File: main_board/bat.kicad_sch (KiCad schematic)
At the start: 50 parts, among them IC1 MP2722GRH-0000-Z, IC2 MP3429GL-Z, IC3 NX3DV42GU, J4 USB_B_Micro, J5 USB_C_Receptacle_USB2.0, U3 ATmega32U4-M, U5 AP2204RB-3.3, U7 INA220AIDGST, Y1 Crystal

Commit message: Rev 1 draft
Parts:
- removed IC3: NX3DV42GU, 000_custom:NX3DV42GU, symbol 000_Custom:NX3DV42GU
- added C65, C66, C67: 1u, Capacitor_SMD:C_0805_2012Metric_Pad1.18x1.45mm_HandSolder, symbol Device:C
- added MOSFET1: STL9P3LLH6, POWERFLAT_3P3X3P3_STM, symbol 000_Custom:STL9P3LLH6
- added R23: 1K, Resistor_SMD:R_0805_2012Metric_Pad1.20x1.40mm_HandSolder, symbol Device:R
- added U8: STUSB4500QTR, 000_custom:STUSB4500, symbol 000_Custom:STUSB4500QTR
- R5: value 0R -> 100K; Field6 (none) -> MCR01MZPF1002; Field7 (none) -> Rohm; Part Description Resistor 2.2K M1005 1% 63mW -> Resistor 10K M1005 1% 63mW
- R9: value 2.2K 1% -> 10K; Field6 (none) -> MCR01MZPF1002; Field7 (none) -> Rohm; Part Description Resistor 2.2K M1005 1% 63mW -> Resistor 10K M1005 1% 63mW; now fitted; now in the parts list
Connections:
- net GND: now also C65.2, C66.2, C67.2, U8.10 (GND), U8.12 (ADDR0), U8.13 (ADDR1), U8.22 (VSYS), U8.25 (EP), U8.6 (RESET), U8.9 (DISCH); no longer R9.2
- net IIC_SCL: now also U8.7 (SCL)
- net IIC_SDA: now also U8.8 (SDA)
- net CC1: no longer names the net of J5.A5 (CC1)
- net CC1: now also U8.1 (CC1DB), U8.2 (CC1); no longer IC1.1 (CC1)
- net CC2: no longer names the net of J5.B5 (CC2)
- net CC2: now also U8.4 (CC2), U8.5 (CC2DB); no longer IC1.22 (CC2_1)
- net OTG_SW: no longer names the net of U3.29 (PB5)
- net PMIC INTERRUPT: no longer names the net of IC1.8 (~{INT})
- net PMIC INTERRUPT: no longer U3.28 (PB4)
- removed net USB2_N: J5.A7 (D-), J5.B7 (D-), R5.1, R5.2
- net USB2_P: no longer names the net of J5.A6 (D+)
- net USB2_P: no longer J5.B6 (D+)
- net USBC_MX2_USB2_N: no longer names the net of IC1.20 (D-)
- net USBC_MX2_USB2_P: no longer names the net of IC1.21 (D+)
- net USB_SW_VCC: no longer names the net of U3.30 (PB6)
- net VIN: no longer names the net of J5.A4 (VBUS), J5.A9 (VBUS), J5.B4 (VBUS), J5.B9 (VBUS)
- net VIN: now also R5.1, C67.1, MOSFET1.1 (S), MOSFET1.2 (S), MOSFET1.3 (S), R23.1, U8.24 (VDD); no longer C19.1, IC1.2 (IN), R9.1
- new net: MOSFET1.4 (G), R5.2, R9.1
- new net: R9.2, U8.16 (VBUS_EN_SNK)
- new net: R23.2, U8.18 (VBUS_VS_DISCH)
- new net: C65.1, U8.21 (VREG_1V2)
- new net: C66.1, U8.23 (VREG_2V7)
- new net: C19.1, IC1.2 (IN), MOSFET1.5 (D), MOSFET1.6 (D), MOSFET1.7 (D), MOSFET1.8 (D)
- no-connect marks 7 -> 22
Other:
- note removed: "Discharge Resistor Needed by some Type C PSUs"
- note removed: "P/N swapped for easier routing"
- moved on the sheet: BT1, C17, C19, C20, C21, C22, C23, C24, C25, C26, C27, C28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

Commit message: Final fixes
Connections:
- net GND: now also U3.36 (PF7), U3.37 (PF6), U3.38 (PF5), U3.39 (PF4), U3.40 (PF1)
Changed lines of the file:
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@@
 	)
 	(junction
+		(at 99.06 256.54)
+		(diameter 0)
+		(color 0 0 0 0)
+	)
+	(junction
 		(at 161.29 115.57)
 		(diameter 0)
@@
 	)
 	(junction
+		(at 99.06 254)
+		(diameter 0)
+		(color 0 0 0 0)
+	)
+	(junction
 		(at 369.57 91.44)
 		(diameter 0)
@@
 	)
 	(junction
+		(at 99.06 259.08)
+		(diameter 0)
+		(color 0 0 0 0)
+	)
+	(junction
 		(at 187.96 60.96)
 		(diameter 0)
@@
 	(wire
 		(pts
+			(xy 99.06 256.54) (xy 99.06 259.08)
+		)
+		(stroke
+			(width 0)
+			(type default)
+		)
+	)
+	(wire
+		(pts
 			(xy 238.76 46.99) (xy 238.76 29.21)
 		)
@@
 	(wire
 		(pts
+			(xy 104.14 261.62) (xy 104.14 259.08)
+		)
+		(stroke
+			(width 0)
+			(type default)
+		)
+	)
+	(wire
+		(pts
 			(xy 265.43 139.7) (xy 265.43 111.76)
 		)
@@
 	(wire
 		(pts
+			(xy 99.06 259.08) (xy 99.06 261.62)
+		)
+		(stroke
+			(width 0)
+			(type default)
+		)
+	)
+	(wire
+		(pts
 			(xy 171.45 90.17) (xy 171.45 91.44)
 		)
@@
 	(wire
 		(pts
+			(xy 99.06 251.46) (xy 99.06 254)
+		)
+		(stroke
+			(width 0)
+			(type default)
+		)
+	)
+	(wire
+		(pts
 			(xy 276.86 91.44) (xy 276.86 129.54)
 		)
@@
 	(wire
 		(pts
+			(xy 104.14 259.08) (xy 99.06 259.08)
+		)
+		(stroke
+			(width 0)
+			(type default)
+		)
+	)
+	(wire
+		(pts
 			(xy 82.55 271.78) (xy 83.82 271.78)
 		)
@@
 	(wire
 		(pts
+			(xy 99.06 254) (xy 99.06 256.54)
+		)
+		(stroke
+			(width 0)
+			(type default)
+		)
+	)
+	(wire
+		(pts
 			(xy 96.52 43.18) (xy 87.63 43.18)
 		)
@@
 					(unit 1)
 				)
+			)
+		)
+	)
+	(symbol
+		(lib_id "power:GND")
+		(at 104.14 261.62 0)
+		(unit 1)
+		(exclude_from_sim no)
+		(in_bom yes)
+		(on_board yes)
+		(dnp no)
+		(property "Reference" "#PWR095"
+			(at 104.14 267.97 0)
+			(effects
+				(font
+					(size 1.27 1.27)
+				)
+				(hide yes)
+			)
+		)
+		(property "Value" "GND"
+			(at 104.14 265.43 0)
+			(effects
+				(font
+					(size 1.27 1.27)
+				)
+			)
+		)
+		(property "Footprint" ""
+			(at 104.14 261.62 0)
+			(effects
+				(font
+					(size 1.27 1.27)
+				)
+				(hide yes)
+			)
+		)
+		(property "Datasheet" ""
+			(at 104.14 261.62 0)
+			(effects
+				(font
+					(size 1.27 1.27)
+				)
+				(hide yes)
+			)
+		)
+		(property "Description" "Power symbol creates a global label with name \"GND\" , ground"
+			(at 104.14 261.62 0)
+			(effects
+				(font
+					(size 1.27 1.27)
+				)
+				(hide yes)
+			)
+		)
+		(pin "1"
+		)
+		(instances
+			(project "main_board"
+				(path "/e63e39d7-6ac0-4ffd-8aa3-1841a4541b55/b84f1a66-243e-4389-abcf-18bc380f8da3"
+					(reference "#PWR095")
+					(unit 1)
+				)

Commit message: Also update schematic
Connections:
- net GND: now also U3.20 (PD2), U3.21 (PD3), U3.22 (PD5)
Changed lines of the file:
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@@
+	)
+	(junction
+		(at 99.06 226.06)
+		(diameter 0)
+		(color 0 0 0 0)
 	)
 	(junction
@@
 	)
 	(junction
-		(at 101.6 233.68)
-		(diameter 0)
-		(color 0 0 0 0)
-	)
-	(junction
 		(at 99.06 254)
 		(diameter 0)
@@
 	)
 	(junction
+		(at 99.06 228.6)
+		(diameter 0)
+		(color 0 0 0 0)
+	)
+	(junction
+		(at 99.06 231.14)
+		(diameter 0)
+		(color 0 0 0 0)
+	)
+	(junction
 		(at 355.6 52.07)
 		(diameter 0)
@@
 	(junction
 		(at 260.35 73.66)
+		(diameter 0)
+		(color 0 0 0 0)
+	)
+	(junction
+		(at 99.06 233.68)
 		(diameter 0)
 		(color 0 0 0 0)
@@
 	(wire
 		(pts
+			(xy 99.06 228.6) (xy 99.06 231.14)
+		)
+		(stroke
+			(width 0)
+			(type default)
+		)
+	)
+	(wire
+		(pts
 			(xy 401.32 46.99) (xy 401.32 199.39)
 		)
@@
 	(wire
 		(pts
-			(xy 99.06 236.22) (xy 101.6 236.22)
-		)
-		(stroke
-			(width 0)
-			(type default)
-		)
-	)
-	(wire
-		(pts
 			(xy 261.62 139.7) (xy 265.43 139.7)
 		)
@@
 	(wire
 		(pts
+			(xy 99.06 226.06) (xy 99.06 228.6)
+		)
+		(stroke
+			(width 0)
+			(type default)
+		)
+	)
+	(wire
+		(pts
 			(xy 346.71 73.66) (xy 346.71 81.28)
 		)
@@
 	(wire
 		(pts
-			(xy 101.6 233.68) (xy 101.6 236.22)
-		)
-		(stroke
-			(width 0)
-			(type default)
-		)
-	)
-	(wire
-		(pts
 			(xy 359.41 46.99) (xy 401.32 46.99)
 		)
@@
 	(wire
 		(pts
+			(xy 99.06 231.14) (xy 99.06 233.68)
+		)
+		(stroke
+			(width 0)
+			(type default)
+		)
+	)
+	(wire
+		(pts
 			(xy 193.04 20.32) (xy 190.5 20.32)
 		)
@@
 	(wire
 		(pts
-			(xy 99.06 228.6) (xy 101.6 228.6)
-		)
-		(stroke
-			(width 0)
-			(type default)
-		)
-	)
-	(wire
-		(pts
 			(xy 403.86 201.93) (xy 358.14 201.93)
 		)
@@
 	(wire
 		(pts
+			(xy 99.06 223.52) (xy 99.06 226.06)
+		)
+		(stroke
+			(width 0)
+			(type default)
+		)
+	)
+	(wire
+		(pts
 			(xy 303.53 91.44) (xy 308.61 91.44)
 		)
@@
 	(wire
 		(pts
-			(xy 101.6 228.6) (xy 101.6 233.68)
-		)
-		(stroke
-			(width 0)
-			(type default)
-		)
-	)
-	(wire
-		(pts
 			(xy 99.06 218.44) (xy 168.91 218.44)
 		)
@@
 	(wire
 		(pts
+			(xy 99.06 231.14) (xy 97.79 231.14)
+		)
+		(stroke
+			(width 0)
+			(type default)
+		)
+	)
+	(wire
+		(pts
 			(xy 281.94 29.21) (xy 281.94 36.83)
 		)
@@
 	(wire
 		(pts
-			(xy 101.6 233.68) (xy 106.68 233.68)
-		)
-		(stroke
-			(width 0)
-			(type default)
-		)
-	)
-	(wire
-		(pts
 			(xy 313.69 101.6) (xy 316.23 101.6)
 		)
@@
 	(wire
 		(pts
-			(xy 99.06 233.68) (xy 101.6 233.68)
-		)
-		(stroke
+			(xy 99.06 233.68) (xy 99.06 236.22)
+		)
+		(stroke
+			(width 0)
+			(type default)
+		)
+	)
+	(wire
+		(pts
+			(xy 99.06 233.68) (xy 106.68 233.68)
+		)
+		(stroke

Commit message: Fix fried USB hub
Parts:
- MOSFET1: footprint POWERFLAT_3P3X3P3_STM -> Package_SON:Diodes_PowerDI3333-8
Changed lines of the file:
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@@
 			)
 		)
-		(property "Footprint" "POWERFLAT_3P3X3P3_STM"
+		(property "Footprint" "Package_SON:Diodes_PowerDI3333-8"
 			(at 195.58 20.32 0)
 			(effects

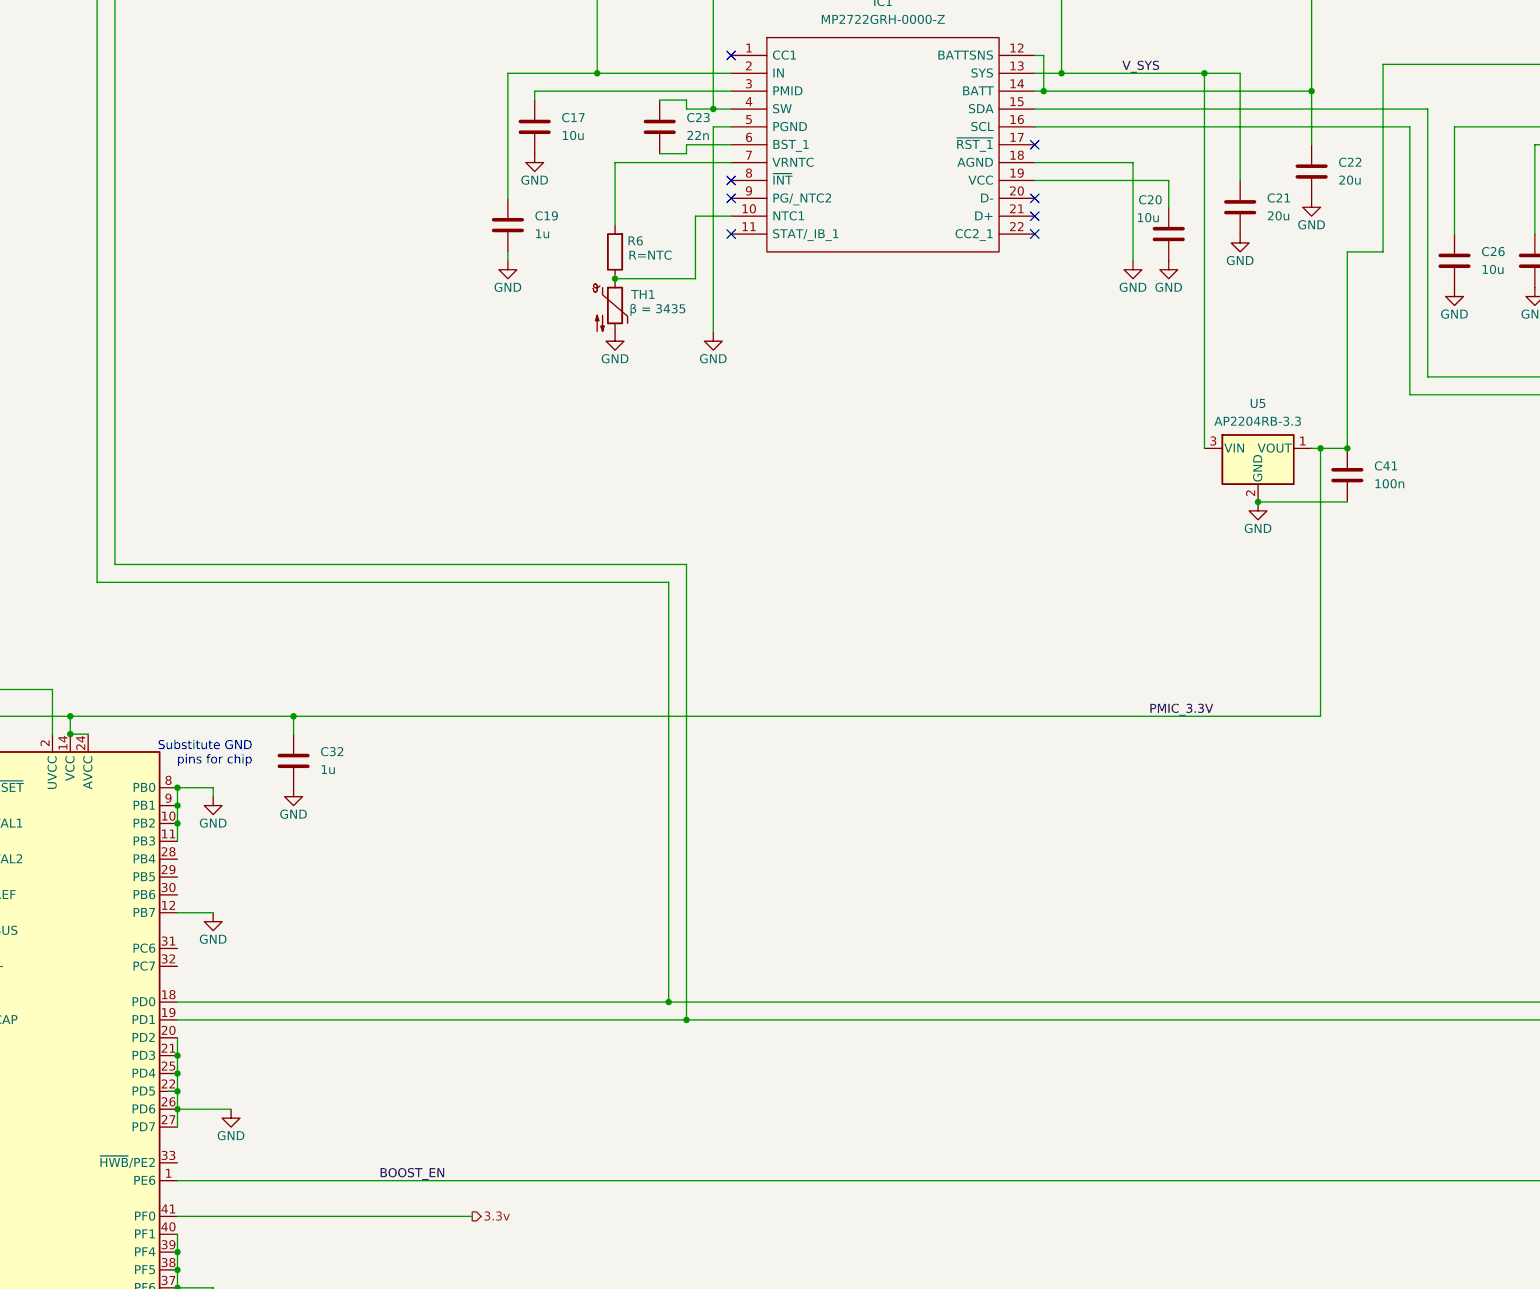
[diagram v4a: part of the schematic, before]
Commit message: Fix 32u4 high power consumption, improve QFN soldering with thick ass solder masks.
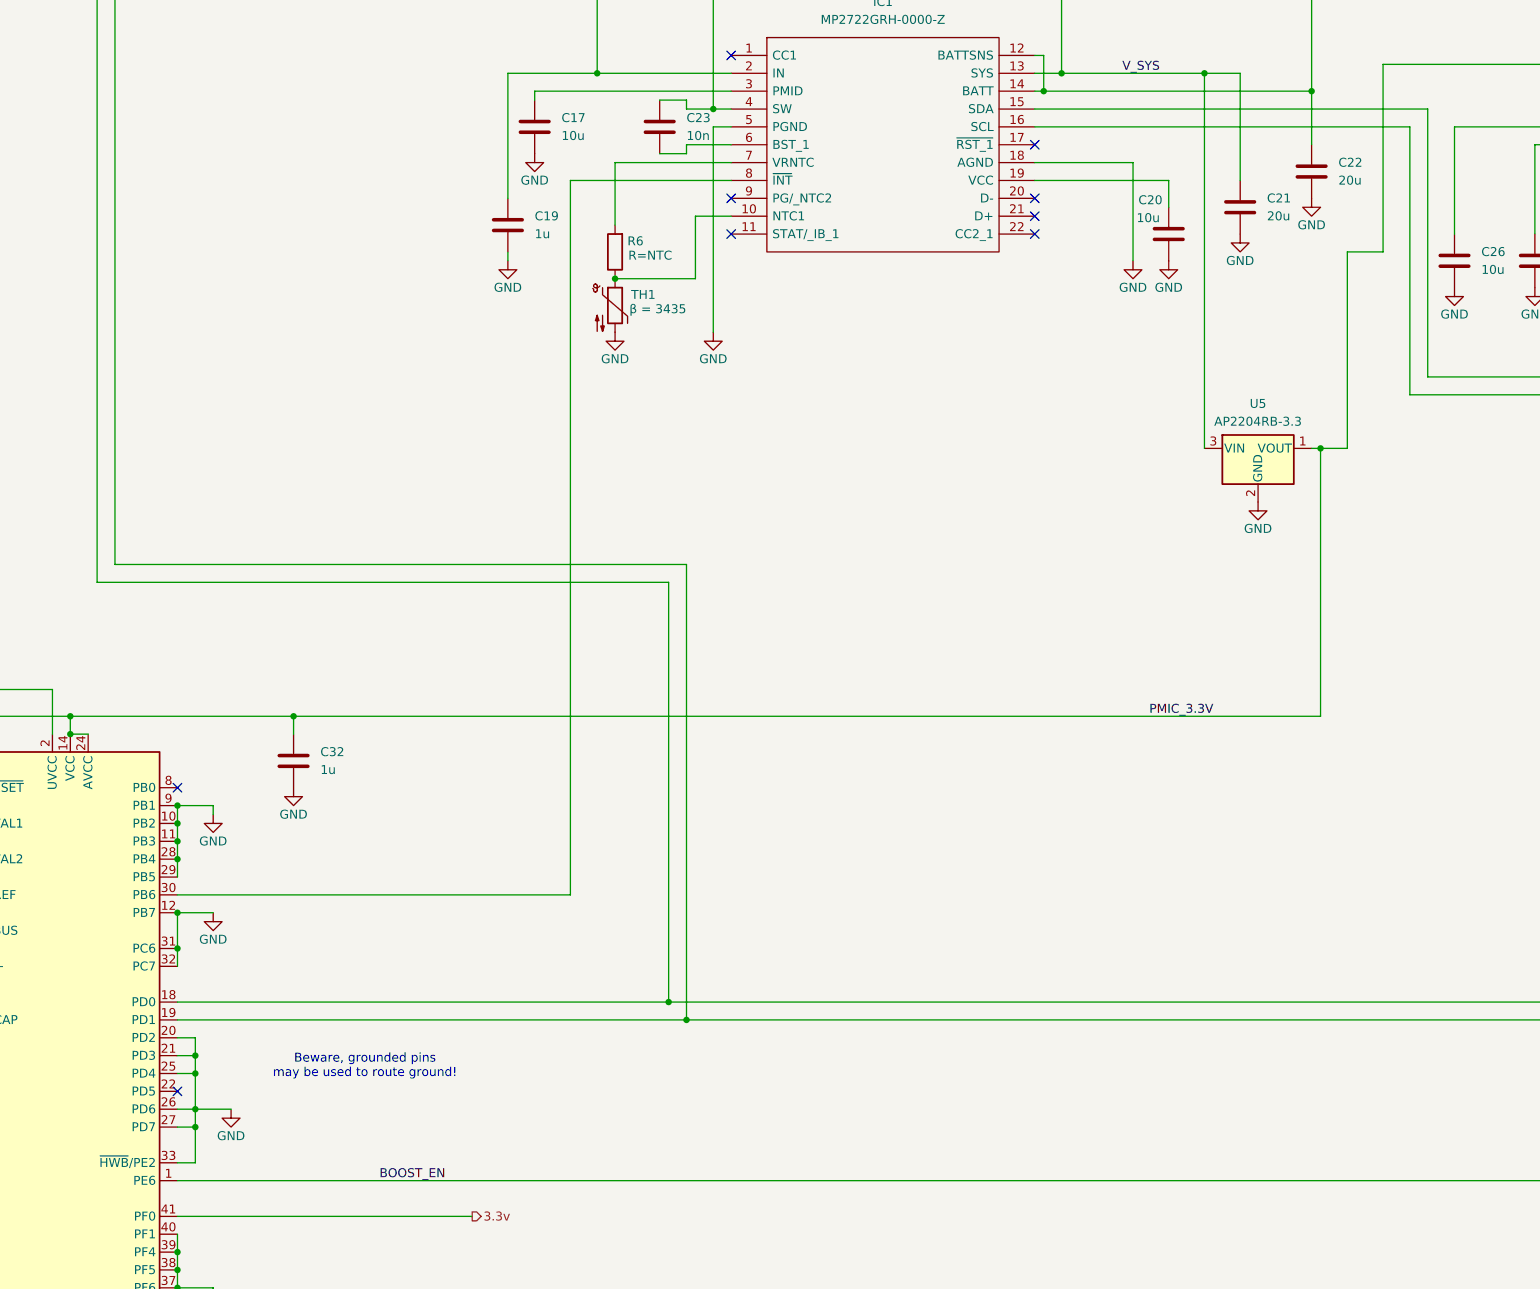
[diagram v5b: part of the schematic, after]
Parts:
- removed C41: 100n, Capacitor_SMD:C_0805_2012Metric_Pad1.18x1.45mm_HandSolder, symbol Device:C
- C23: value 22n -> 10n
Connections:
- net GND: now also U3.28 (PB4), U3.29 (PB5), U3.31 (PC6), U3.32 (PC7), U3.33 (~{HWB}/PE2); no longer U3.22 (PD5), U3.8 (PB0)
- net at IC1.8 (~{INT}): now also U3.30 (PB6)
- no-connect marks 22 -> 23
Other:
- note added: "Beware, grounded pins may be used to route ground!"
- note removed: "Substitute GND pins for chip"

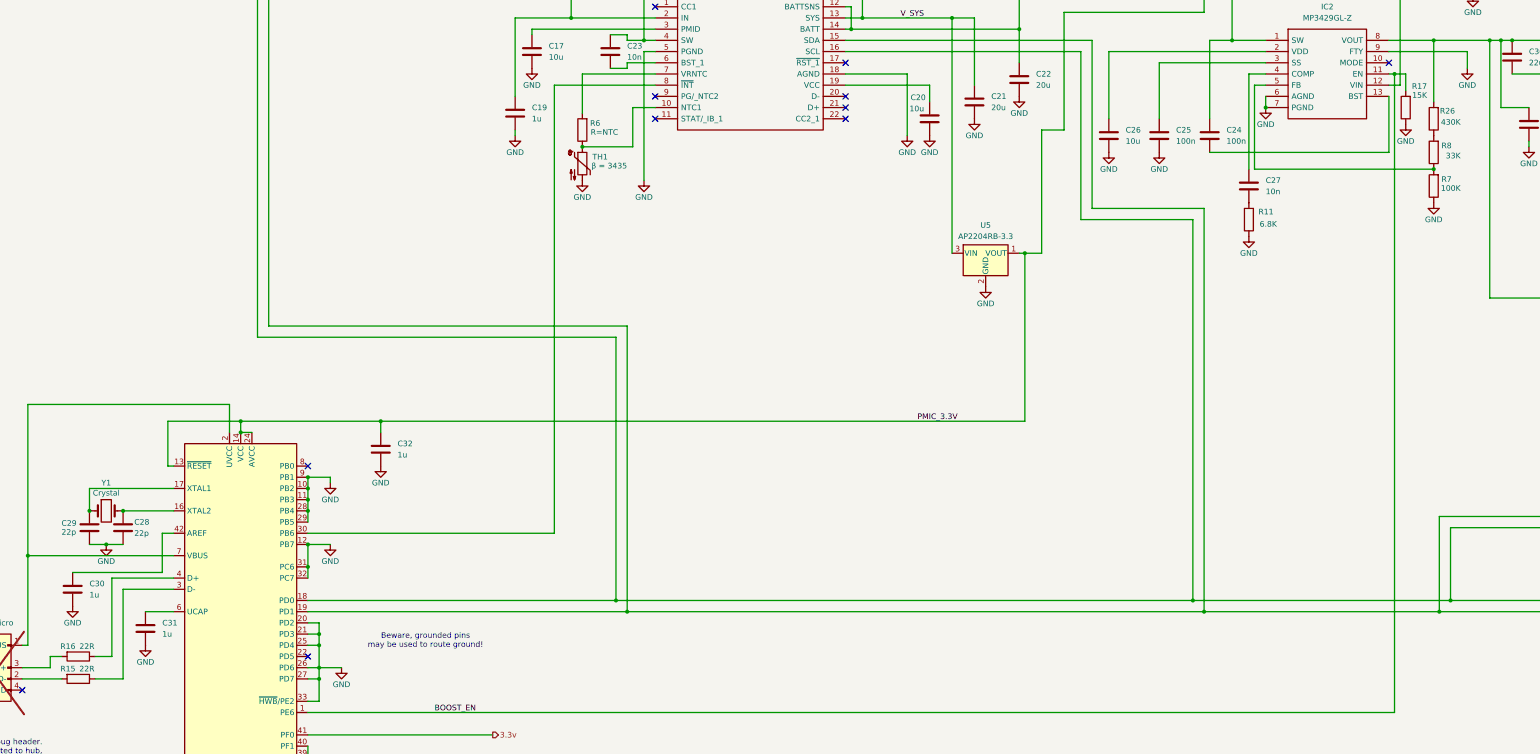
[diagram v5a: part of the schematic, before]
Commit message: Fix bad output voltage
For some reason I got 5V with previous values on prototype. Weird...
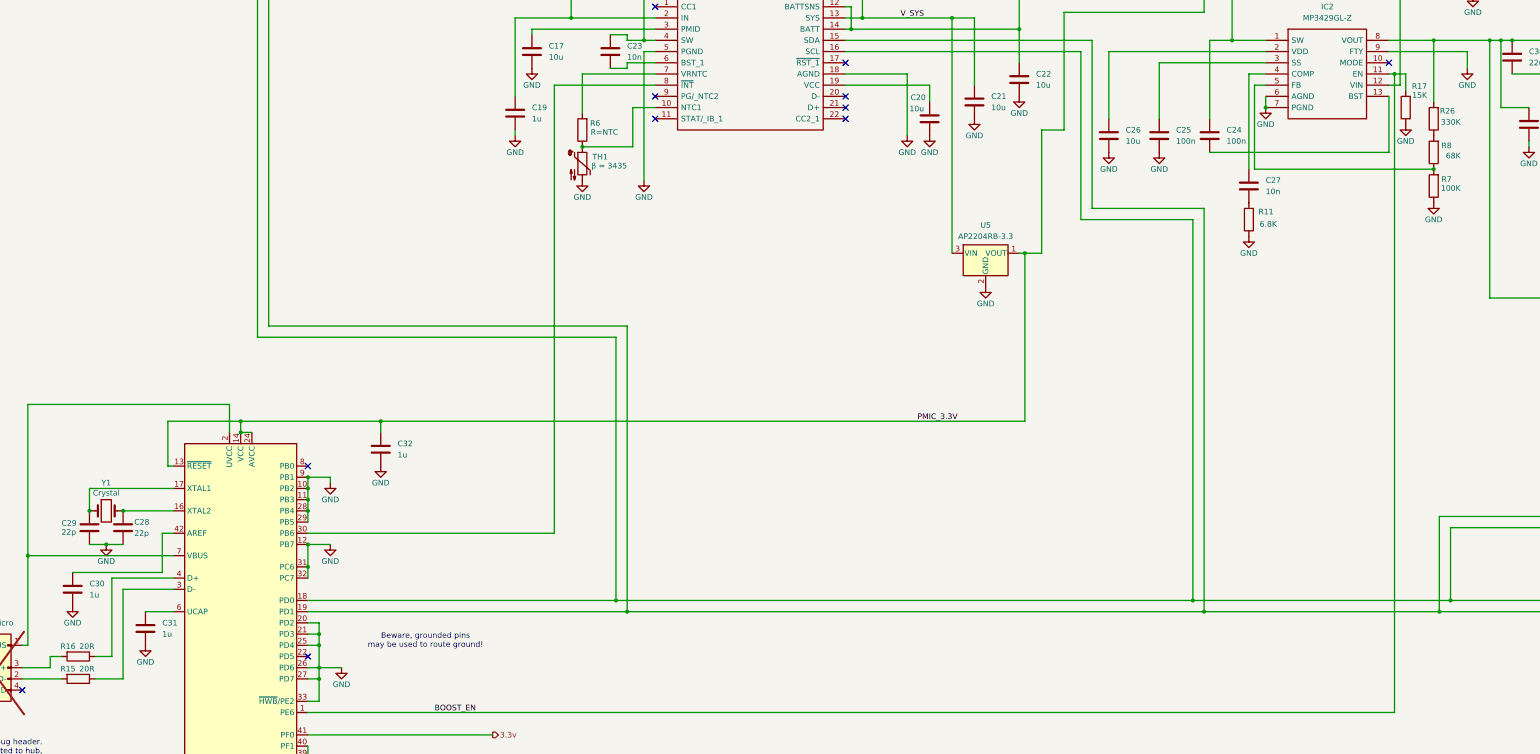
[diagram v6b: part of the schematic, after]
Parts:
- C21, C22: value 20u -> 10u
- R15, R16: value 22R -> 20R
- R26: value 430K -> 330K
- R8: value 33K -> 68K
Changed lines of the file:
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@@
 			)
 		)
-		(property "Value" "20u"
+		(property "Value" "10u"
 			(at 254 106.6799 0)
 			(effects
@@
 			)
 		)
-		(property "Value" "20u"
+		(property "Value" "10u"
 			(at 264.16 101.5999 0)
 			(effects
@@
 			)
 		)
-		(property "Value" "33K"
+		(property "Value" "68K"
 			(at 360.426 117.602 0)
 			(effects
@@
 			)
 		)
-		(property "Value" "22R"
+		(property "Value" "20R"
 			(at 47.244 228.854 90)
 			(effects
@@
 			)
 		)
-		(property "Value" "22R"
+		(property "Value" "20R"
 			(at 47.244 233.934 90)
 			(effects
@@
 			)
 		)
-		(property "Value" "430K"
+		(property "Value" "330K"
 			(at 360.426 109.982 0)
 			(effects
